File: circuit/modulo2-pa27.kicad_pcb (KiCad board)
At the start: 2 copper layers, 105 x 47 mm, 48 parts, among them J1 CONN_01X02, J2 POWER, J3 CONN_01X04, J4 JACK_MONO, J5 HOLE, J7 HOLE, SW1 bright, U1 OPA2134, U2 OPA2134, U3 TLE2426

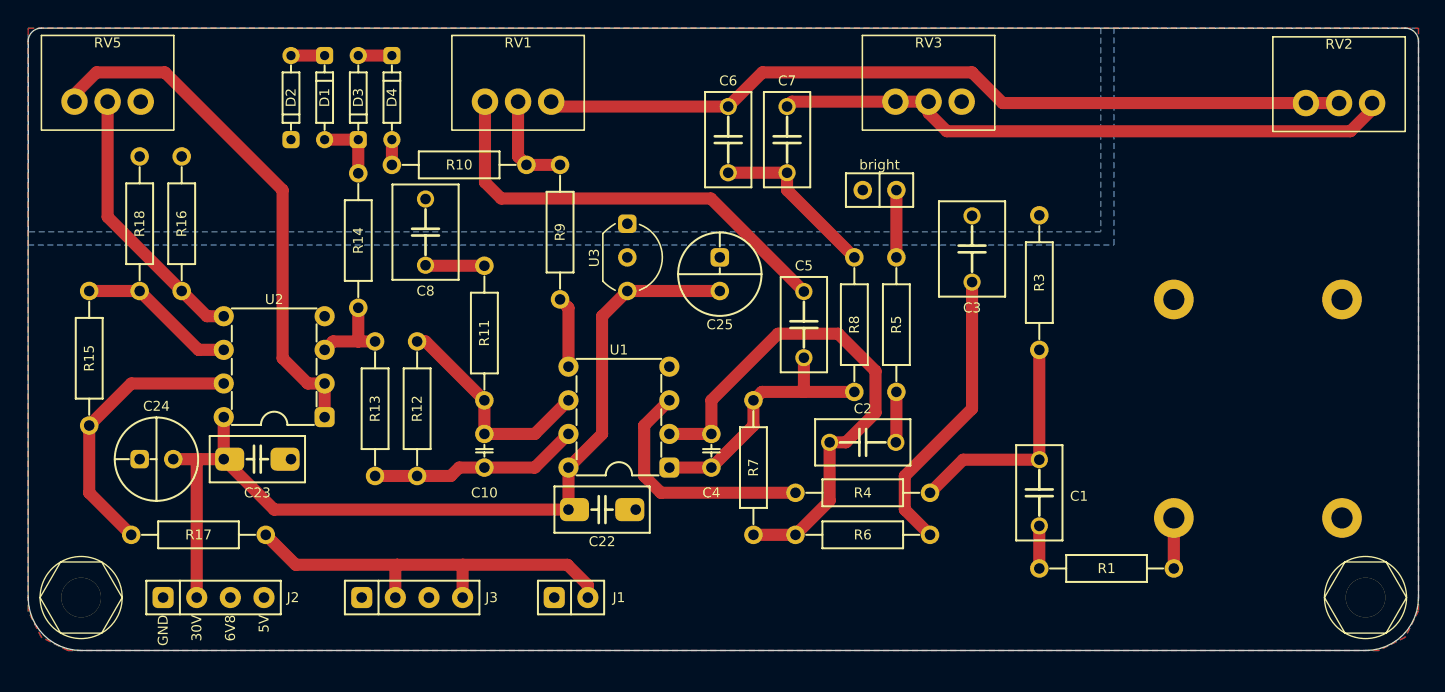
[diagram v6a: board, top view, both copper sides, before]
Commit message: further routing of FV-1
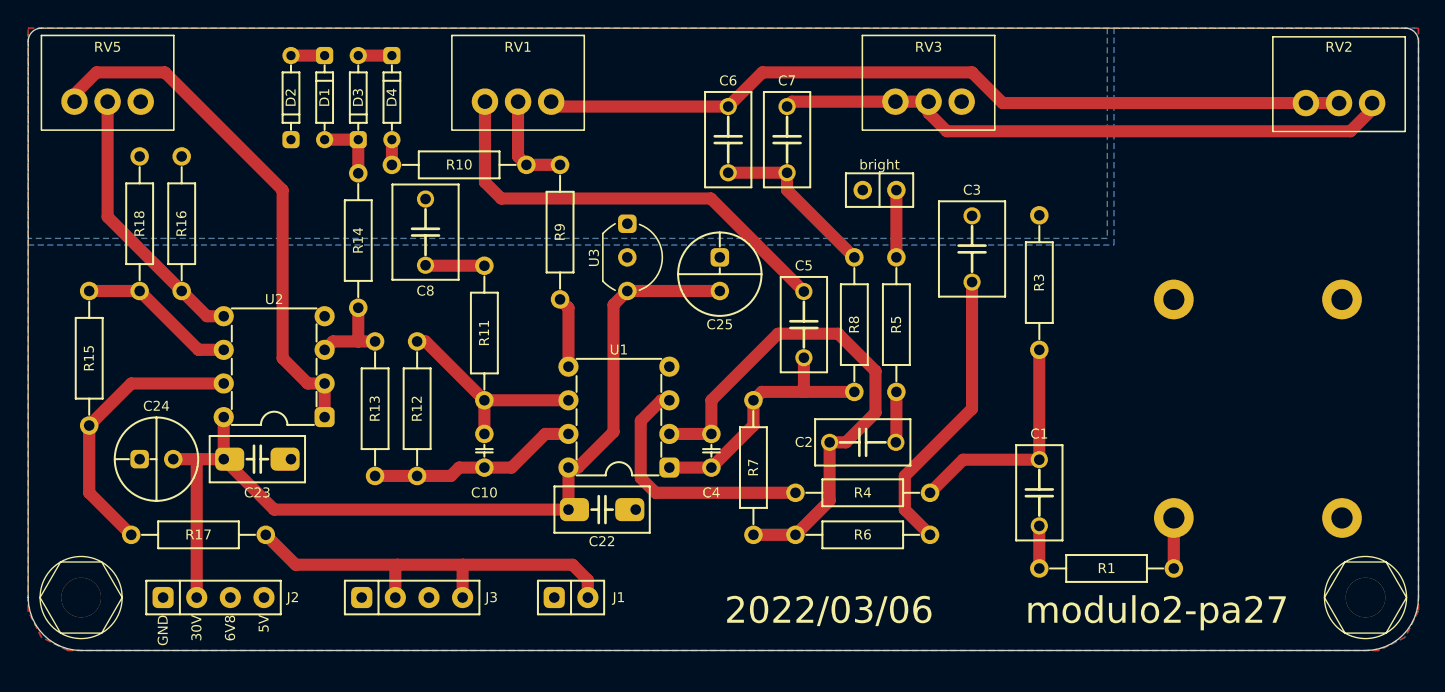
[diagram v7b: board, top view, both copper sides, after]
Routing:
- net Net-(C10-Pad1): track 16.9 -> 15.8 mm
- net Net-(R4-Pad1): track 18.5 -> 19.3 mm
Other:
- board text added: "2022/03/06"
- board text added: "modulo2-pa27"
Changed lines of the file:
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@@
     (property "Sheetname" "")
     (attr through_hole)
-    (fp_text reference "C3" (at 4.445 0) (layer "F.SilkS")
+    (fp_text reference "C3" (at -4.445 0) (layer "F.SilkS")
       (effects (font (size 0.75 0.75) (thickness 0.15)))
     )
@@
     (property "Sheetname" "")
     (attr through_hole)
-    (fp_text reference "C2" (at 0 2.54) (layer "F.SilkS")
+    (fp_text reference "C2" (at 4.445 0) (layer "F.SilkS")
       (effects (font (size 0.75 0.75) (thickness 0.15)))
     )
@@
     (property "Sheetname" "")
     (attr through_hole)
-    (fp_text reference "RV2" (at 0 4.445) (layer "F.SilkS")
+    (fp_text reference "RV2" (at 0 4.22) (layer "F.SilkS")
       (effects (font (size 0.75 0.75) (thickness 0.15)))
     )
@@
     (property "Sheetname" "")
     (attr through_hole)
-    (fp_text reference "RV3" (at 0 4.445) (layer "F.SilkS")
+    (fp_text reference "RV3" (at 0 4.115) (layer "F.SilkS")
       (effects (font (size 0.75 0.75) (thickness 0.15)))
     )
@@
     (property "Sheetname" "")
     (attr through_hole)
-    (fp_text reference "C1" (at -0.254 3) (layer "F.SilkS")
+    (fp_text reference "C1" (at 4.445 0) (layer "F.SilkS")
       (effects (font (size 0.75 0.75) (thickness 0.15)))
     )
@@
     (property "Sheetname" "")
     (attr through_hole)
-    (fp_text reference "RV1" (at 0 4.445) (layer "F.SilkS")
+    (fp_text reference "RV1" (at 0.005 4.115) (layer "F.SilkS")
       (effects (font (size 0.75 0.75) (thickness 0.15)))
     )
@@
     (property "Sheetname" "")
     (attr through_hole)
-    (fp_text reference "RV5" (at 0 4.445) (layer "F.SilkS")
+    (fp_text reference "RV5" (at 0 4.115) (layer "F.SilkS")
       (effects (font (size 0.75 0.75) (thickness 0.15)))
     )
@@
   (gr_line (start 51 50) (end 154 50) (layer "Edge.Cuts") (width 0.05))
   (gr_arc (start 155 93) (mid 153.828427 95.828427) (end 151 97) (layer "Edge.Cuts") (width 0.05))
-  (segment (start 93.345 80.645) (end 90.805 83.185) (width 0.9144) (layer "F.Cu") (net 1))
+  (gr_text "2022/03/06" (at 110.49 93.98) (layer "F.SilkS")
+    (effects (font (size 2 2) (thickness 0.3)))
+  )
+  (gr_text "modulo2-pa27" (at 135.255 93.98) (layer "F.SilkS")
+    (effects (font (size 2 2) (thickness 0.3)))
+  )
+  (segment (start 94.2086 70.8914) (end 94.2086 80.4926) (width 0.9144) (layer "F.Cu") (net 1))
   (segment (start 64.77 82.55) (end 62.865 82.55) (width 0.9144) (layer "F.Cu") (net 1))
   (segment (start 90.805 83.185) (end 90.805 86.36) (width 0.9144) (layer "F.Cu") (net 1))
+  (segment (start 94.2086 80.4926) (end 91.5162 83.185) (width 0.9144) (layer "F.Cu") (net 1))
   (segment (start 62.73 93) (end 62.73 82.685) (width 0.9144) (layer "F.Cu") (net 1))
-  (segment (start 93.345 71.755) (end 93.345 80.645) (width 0.9144) (layer "F.Cu") (net 1))
   (segment (start 102.235 69.85) (end 95.25 69.85) (width 0.9144) (layer "F.Cu") (net 1))
-  (segment (start 95.25 69.85) (end 93.345 71.755) (width 0.9144) (layer "F.Cu") (net 1))
   (segment (start 64.77 82.55) (end 68.58 86.36) (width 0.9144) (layer "F.Cu") (net 1))
+  (segment (start 95.25 69.85) (end 94.2086 70.8914) (width 0.9144) (layer "F.Cu") (net 1))
   (segment (start 62.865 82.55) (end 60.96 82.55) (width 0.9144) (layer "F.Cu") (net 1))
+  (segment (start 91.5162 83.185) (end 90.805 83.185) (width 0.9144) (layer "F.Cu") (net 1))
   (segment (start 62.73 82.685) (end 62.865 82.55) (width 0.9144) (layer "F.Cu") (net 1))
   (segment (start 68.58 86.36) (end 90.805 86.36) (width 0.9144) (layer "F.Cu") (net 1))
@@
   (segment (start 84.455 67.945) (end 80.05 67.945) (width 0.9144) (layer "F.Cu") (net 11))
   (segment (start 80.05 67.945) (end 80.01 67.905) (width 0.9144) (layer "F.Cu") (net 11))
-  (segment (start 88.265 80.645) (end 84.455 80.645) (width 0.9144) (layer "F.Cu") (net 12))
+  (segment (start 90.805 78.105) (end 84.455 78.105) (width 0.9144) (layer "F.Cu") (net 12))
   (segment (start 80.01 73.66) (end 84.455 78.105) (width 0.9144) (layer "F.Cu") (net 12))
   (segment (start 79.375 73.66) (end 80.01 73.66) (width 0.9144) (layer "F.Cu") (net 12))
   (segment (start 84.455 80.645) (end 84.455 78.105) (width 0.9144) (layer "F.Cu") (net 12))
-  (segment (start 90.805 78.105) (end 88.265 80.645) (width 0.9144) (layer "F.Cu") (net 12))
   (segment (start 84.455 83.185) (end 82.55 83.185) (width 0.9144) (layer "F.Cu") (net 13))
+  (segment (start 84.455 83.185) (end 86.5124 83.185) (width 0.9144) (layer "F.Cu") (net 13))
   (segment (start 81.915 83.82) (end 79.375 83.82) (width 0.9144) (layer "F.Cu") (net 13))
+  (segment (start 86.5124 83.185) (end 89.0524 80.645) (width 0.9144) (layer "F.Cu") (net 13))
   (segment (start 76.2 83.82) (end 79.375 83.82) (width 0.9144) (layer "F.Cu") (net 13))
-  (segment (start 88.265 83.185) (end 90.805 80.645) (width 0.9144) (layer "F.Cu") (net 13))
-  (segment (start 84.455 83.185) (end 88.265 83.185) (width 0.9144) (layer "F.Cu") (net 13))
+  (segment (start 89.0524 80.645) (end 90.805 80.645) (width 0.9144) (layer "F.Cu") (net 13))
   (segment (start 82.55 83.185) (end 81.915 83.82) (width 0.9144) (layer "F.Cu") (net 13))
   (segment (start 77.8764 90.5256) (end 70.2056 90.5256) (width 0.9144) (layer "F.Cu") (net 14))
-  (segment (start 92.27 92.0668) (end 90.7288 90.5256) (width 0.9144) (layer "F.Cu") (net 14))
+  (segment (start 91.1098 90.5256) (end 82.8294 90.5256) (width 0.9144) (layer "F.Cu") (net 14))
   (segment (start 70.2056 90.5256) (end 67.945 88.265) (width 0.9144) (layer "F.Cu") (net 14))
+  (segment (start 92.27 91.6858) (end 91.1098 90.5256) (width 0.9144) (layer "F.Cu") (net 14))
   (segment (start 82.8294 90.5256) (end 77.8764 90.5256) (width 0.9144) (layer "F.Cu") (net 14))
   (segment (start 82.81 90.545) (end 82.8294 90.5256) (width 0.9144) (layer "F.Cu") (net 14))
-  (segment (start 90.7288 90.5256) (end 82.8294 90.5256) (width 0.9144) (layer "F.Cu") (net 14))
   (segment (start 77.73 90.672) (end 77.8764 90.5256) (width 0.9144) (layer "F.Cu") (net 14))
   (segment (start 82.81 93) (end 82.81 90.545) (width 0.9144) (layer "F.Cu") (net 14))
-  (segment (start 92.27 93) (end 92.27 92.0668) (width 0.9144) (layer "F.Cu") (net 14))
+  (segment (start 92.27 93) (end 92.27 91.6858) (width 0.9144) (layer "F.Cu") (net 14))
   (segment (start 77.73 93) (end 77.73 90.672) (width 0.9144) (layer "F.Cu") (net 14))
   (segment (start 77.47 58.42) (end 77.47 60.325) (width 0.9144) (layer "F.Cu") (net 15))
@@
   (segment (start 74.93 52.07) (end 77.47 52.07) (width 0.9144) (layer "F.Cu") (net 22))
   (segment (start 136.525 90.805) (end 136.525 86.99) (width 0.9144) (layer "F.Cu") (net 23))
-  (segment (start 96.52 80.01) (end 96.52 83.82) (width 0.9144) (layer "F.Cu") (net 24))
-  (segment (start 98.425 78.105) (end 96.52 80.01) (width 0.9144) (layer "F.Cu") (net 24))
-  (segment (start 97.79 85.09) (end 107.95 85.09) (width 0.9144) (layer "F.Cu") (net 24))
-  (segment (start 96.52 83.82) (end 97.79 85.09) (width 0.9144) (layer "F.Cu") (net 24))
+  (segment (start 97.8154 78.105) (end 96.266 79.6544) (width 0.9144) (layer "F.Cu") (net 24))
+  (segment (start 98.425 78.105) (end 97.8154 78.105) (width 0.9144) (layer "F.Cu") (net 24))
+  (segment (start 96.266 83.9724) (end 97.3836 85.09) (width 0.9144) (layer "F.Cu") (net 24))
+  (segment (start 97.3836 85.09) (end 107.95 85.09) (width 0.9144) (layer "F.Cu") (net 24))
+  (segment (start 96.266 79.6544) (end 96.266 83.9724) (width 0.9144) (layer "F.Cu") (net 24))
   (segment (start 90.805 75.565) (end 90.805 71.12) (width 0.9144) (layer "F.Cu") (net 25))
   (segment (start 90.805 71.12) (end 90.17 70.485) (width 0.9144) (layer "F.Cu") (net 25))
@@
     (polygon
       (pts
-        (xy 131 65.38)
-        (xy 50 65.38)
+        (xy 131.5 65.88)
+        (xy 50 65.88)
         (xy 50 50)
-        (xy 131 50)
+        (xy 131.5 50)
       )
     )

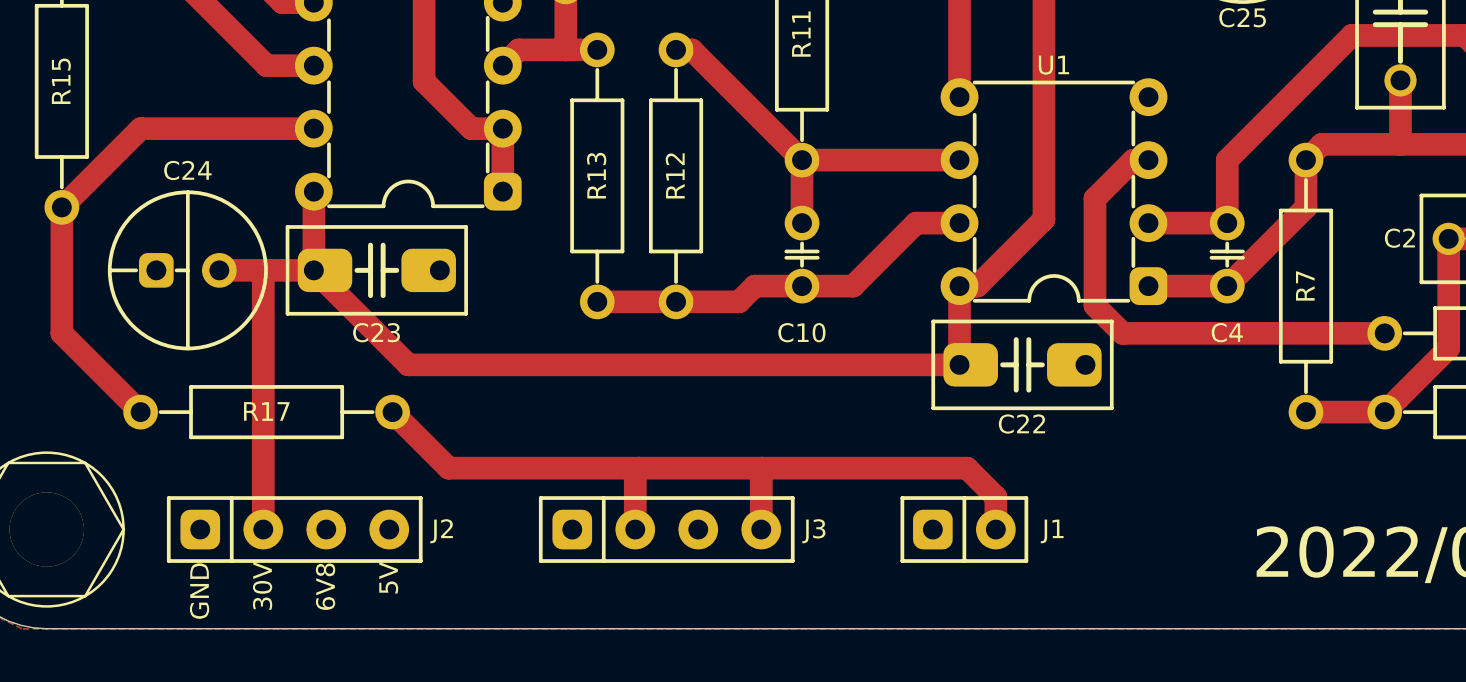
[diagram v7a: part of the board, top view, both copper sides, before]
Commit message: no more assembler; more routing
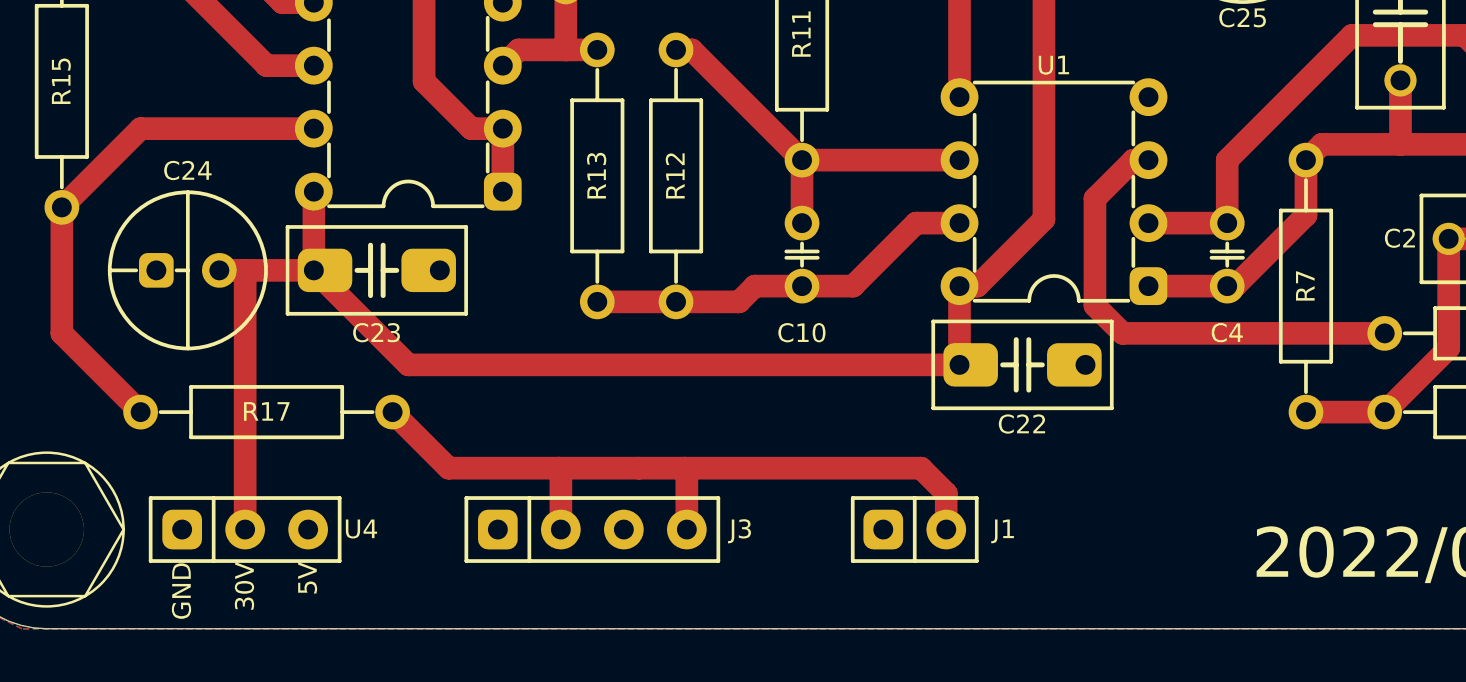
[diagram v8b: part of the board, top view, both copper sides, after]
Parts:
- removed J2: POWER, myAmp:POWER
- added U4: POWER, myAmp:PWR_CONN, F.Cu at (62.0, 93.0)
- moved J3 3.00 mm to (76.0, 93.0)
- moved J1 2.00 mm to (89.0, 93.0)
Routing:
- net /PA_OUT: track 32.1 -> 30.2 mm
